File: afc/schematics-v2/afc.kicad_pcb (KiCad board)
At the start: 2 copper layers, 116.8 x 67.3 mm, 16 parts

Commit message: adding v2 schematics
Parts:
- removed ENV2: FAN_H4, Connector:FanPinHeader_1x04_P2.54mm_Vertical
- added Ce: C_Disc_D10.5mm_W5.0mm_P10.00mm, Capacitor_THT:C_Disc_D10.5mm_W5.0mm_P10.00mm, F.Cu at (162.6, 87.5)
- added REF**: R_Axial_DIN0207_L6.3mm_D2.5mm_P10.16mm_Horizontal, Resistor_THT:R_Axial_DIN0207_L6.3mm_D2.5mm_P10.16mm_Horizontal, F.Cu at (135.3, 54.6)
- added REF**: R_Axial_DIN0207_L6.3mm_D2.5mm_P10.16mm_Horizontal, Resistor_THT:R_Axial_DIN0207_L6.3mm_D2.5mm_P10.16mm_Horizontal, F.Cu at (180.3, 77.5)
- added REF**: R_Axial_DIN0207_L6.3mm_D2.5mm_P10.16mm_Horizontal, Resistor_THT:R_Axial_DIN0207_L6.3mm_D2.5mm_P10.16mm_Horizontal, F.Cu at (150.5, 54.6)
- added REF**: R_Axial_DIN0207_L6.3mm_D2.5mm_P10.16mm_Horizontal, Resistor_THT:R_Axial_DIN0207_L6.3mm_D2.5mm_P10.16mm_Horizontal, F.Cu at (120.0, 54.6)
- moved FAN02 27.4 mm to (146.7, 64.8), turned to 180 degrees
- moved FAN03 27.4 mm to (131.4, 64.8), turned to 180 degrees
- moved FAN04 27.4 mm to (116.2, 64.8), turned to 180 degrees
- moved FAN01 27.4 mm to (161.9, 64.8), turned to 180 degrees
- moved ? 20.4 mm to (184.8, 73.7)
- moved ? 20.4 mm to (190.0, 68.6)
- moved ATX2 20.4 mm to (184.8, 83.8)
- moved ATX3 20.4 mm to (184.8, 78.7)
- moved ? 20.4 mm to (184.8, 88.9)
- moved ? 20.4 mm to (190.0, 94.0)
- moved ? 17.0 mm to (108.0, 114.3)
- moved PCIe_MNT_TOP 17.0 mm to (108.0, 76.3)
- moved ESP32_A 14.2 mm to (127.0, 87.6)
- moved ESP32_B 14.0 mm to (127.0, 106.7)
- moved ENV1 8.03 mm to (162.6, 94.0)
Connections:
- ESP32_A pad 1: PWM1 -> TACHO1
- ESP32_A pad 2: TACHO1 -> PWM1
- ESP32_A pad 3: PWM2 -> TACHO2
- ESP32_A pad 4: TACHO2 -> PWM2
- ESP32_A pad 5: PWM3 -> TACHO3
- ESP32_A pad 6: TACHO3 -> PWM3
- ESP32_B pad 10: SDA_1 -> (no net)
- ESP32_B pad 11: SDA_2 -> (no net)
- ESP32_B pad 12: SCL_2 -> SCL_1
- ESP32_B pad 13: (no net) -> SDA_1
- ESP32_B pad 9: SCL_1 -> (no net)
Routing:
- net 12V: track 226.4 -> 121.2 mm
- net SDA_2: track 74.7 -> 0.00 mm
- net GND: track 245.7 -> 172.7 mm
- net SCL_2: track 68.5 -> 0.00 mm
- net TACHO2: track 72.4 -> 25.8 mm
- net TACHO1: track 84.4 -> 38.2 mm
- net PWM1: track 81.6 -> 37.4 mm
- net PWM2: track 69.6 -> 25.8 mm
- net TACHO3: track 60.0 -> 24.2 mm
- net 3V3: track 60.2 -> 25.2 mm
- net PWM3: track 57.9 -> 24.2 mm
- net SDA_1: track 53.0 -> 24.7 mm
- net TACHO4: track 82.8 -> 54.7 mm
- net SCL_1: track 57.7 -> 29.7 mm
- net PWM4: track 68.0 -> 54.7 mm
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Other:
- board size 116.8 x 67.3 mm -> 90.2 x 67.3 mm
- board text removed: "ESP32-S3-ZERO"

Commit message: improvements on PCB design
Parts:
- moved REF** 22.7 mm to (140.3, 64.8), turned to 180 degrees
- moved REF** 22.7 mm to (155.6, 64.8), turned to 180 degrees
- moved REF** 22.7 mm to (170.8, 64.8), turned to 180 degrees
- moved FAN03 13.2 mm to (142.2, 57.1)
- moved FAN04 13.2 mm to (127.0, 57.1)
- moved FAN01 13.2 mm to (172.7, 57.1)
- moved FAN02 13.2 mm to (157.5, 57.1)
- moved ENV1 13.0 mm to (175.3, 91.4)
- moved PCIe_MNT_TOP 9.24 mm to (113.0, 68.6)
- moved ? 9.16 mm to (113.0, 106.7)
- moved ? 6.38 mm to (190.6, 87.6)
- moved ? 6.38 mm to (185.4, 82.5)
- moved ESP32_B 6.38 mm to (127.6, 100.3)
- moved ? 6.38 mm to (190.6, 62.2)
- moved ESP32_A 6.38 mm to (127.7, 81.3)
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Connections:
- REF** pad 1: GND -> 12V (x3)
- REF** pad 2: GND -> 12V (x3)
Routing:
- net 12V: track 121.2 -> 73.6 mm
- net 3V3: track 25.2 -> 39.9 mm
- net SDA_1: track 24.7 -> 36.9 mm
- net SCL_1: track 29.7 -> 41.2 mm
- net TACHO2: track 25.8 -> 37.2 mm
- net PWM2: track 25.8 -> 37.2 mm
- net TACHO1: track 38.2 -> 48.1 mm
- net PWM1: track 37.4 -> 47.3 mm
- net TACHO4: track 54.7 -> 46.6 mm
- net PWM4: track 54.7 -> 46.6 mm
- net PWM3: track 24.2 -> 27.0 mm
- net TACHO3: track 24.2 -> 27.0 mm
- net 5V: track 65.4 -> 66.9 mm
- net GND: track 172.7 -> 173.6 mm
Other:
- board size 90.2 x 67.3 mm -> 85.1 x 59.7 mm

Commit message: more cleanup
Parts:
- moved ENV1 3.59 mm to (172.7, 88.9)
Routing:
- net 5V: track 66.9 -> 76.9 mm
- net 12V: track 73.6 -> 82.8 mm
- net GND: track 173.6 -> 182.7 mm
- net 3V3: track 39.9 -> 48.9 mm
- net SDA_1: track 36.9 -> 33.3 mm
- net SCL_1: track 41.2 -> 37.6 mm
- net TACHO1: track 48.1 -> 47.3 mm
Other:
- outline, holes or cut-outs redrawn

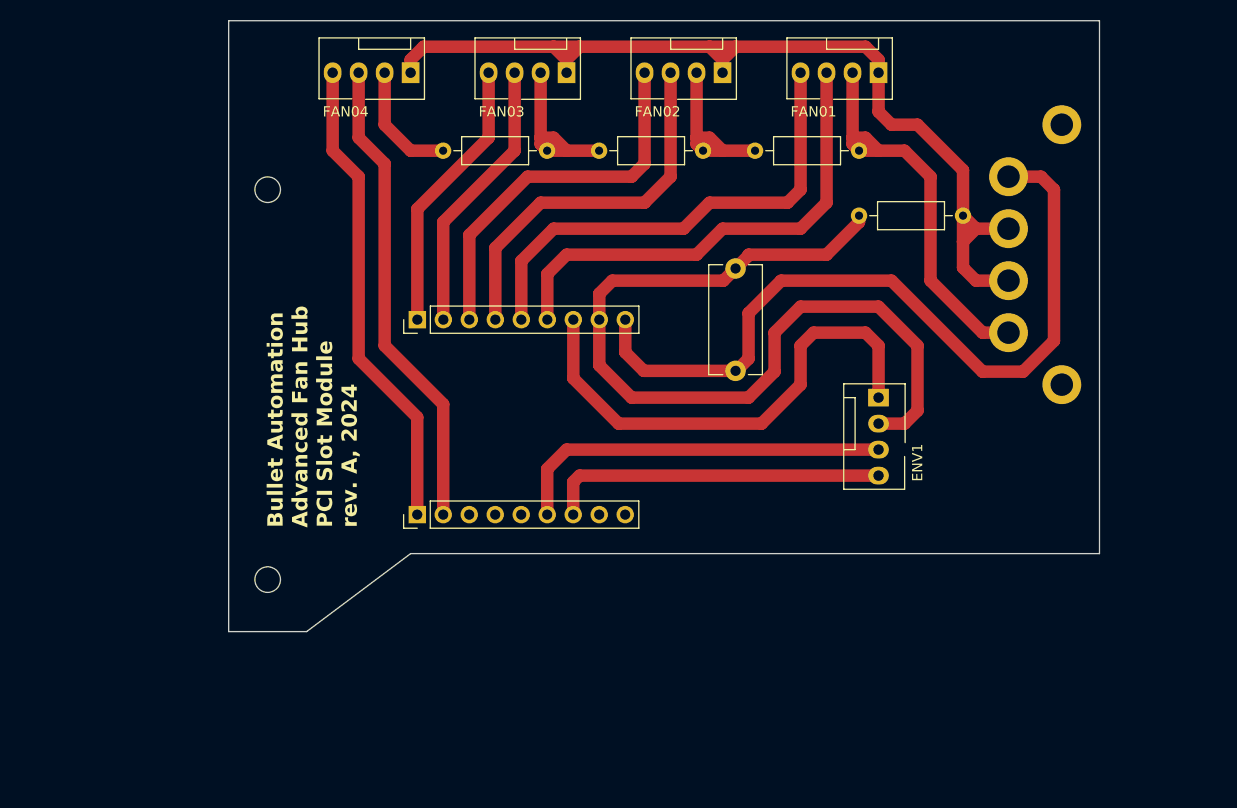
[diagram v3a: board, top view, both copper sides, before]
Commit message: ground plane for schematic
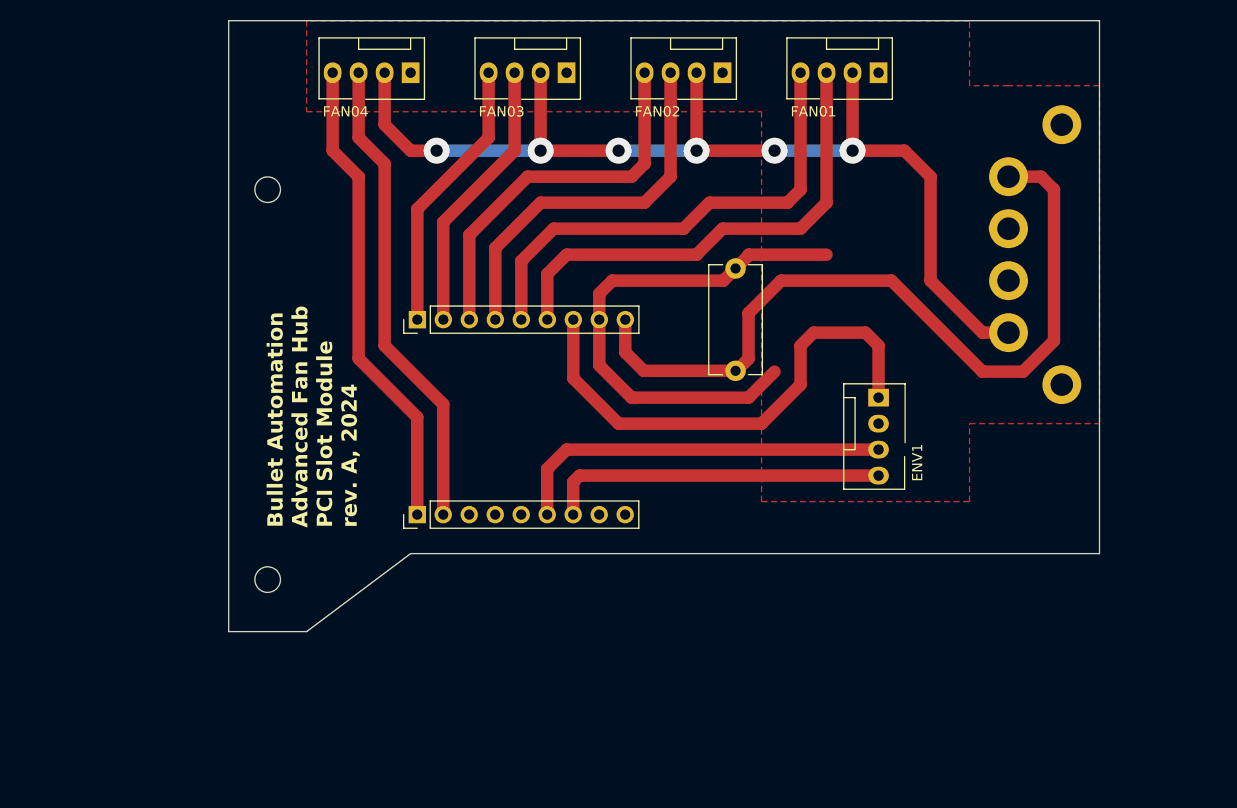
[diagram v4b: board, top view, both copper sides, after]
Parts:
- removed REF** (x4): R_Axial_DIN0207_L6.3mm_D2.5mm_P10.16mm_Horizontal, Resistor_THT:R_Axial_DIN0207_L6.3mm_D2.5mm_P10.16mm_Horizontal
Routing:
- net GND: track 182.7 -> 51.7 mm
- net 12V: track 82.8 -> 103.3 mm, vias 0 -> 6
- added copper zone on F.Cu, net GND

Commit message: updating schematic
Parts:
- moved ESP32_B 3.81 mm to (127.6, 96.5)
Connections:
- ESP32_B pad 12: SCL_1 -> SDA_1
- ESP32_B pad 13: SDA_1 -> SCL_1
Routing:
- net SCL_1: track 37.6 -> 32.0 mm
- net TACHO4: track 46.6 -> 42.8 mm
- net PWM4: track 46.6 -> 42.8 mm
- net SDA_1: track 33.3 -> 37.0 mm
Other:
- board text added: "AFC R2 - Bullet Automation"
- board text removed: "Bullet Automation Advanced Fan Hub PCI Slot Module rev. A, 2024"
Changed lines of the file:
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@@
 	(footprint "Connector_PinHeader_2.54mm:PinHeader_1x09_P2.54mm_Vertical"
 		(layer "F.Cu")
-		(at 127.645 100.33 90)
+		(at 127.645 96.52 90)
 		(descr "Through hole straight pin header, 1x09, 2.54mm pitch, single row")
 		(tags "Through hole pin header THT 1x09 2.54mm single row")
@@
 			(layers "*.Cu" "*.Mask")
 			(remove_unused_layers no)
-			(net 13 "SCL_1")
+			(net 14 "SDA_1")
 		)
 		(pad "13" thru_hole oval
@@
 			(layers "*.Cu" "*.Mask")
 			(remove_unused_layers no)
-			(net 14 "SDA_1")
+			(net 13 "SCL_1")
 		)
 		(pad "RX" thru_hole oval
@@
 		)
 	)
-	(gr_text "Bullet Automation\nAdvanced Fan Hub\nPCI Slot Module\nrev. A, 2024"
-		(at 121.92 101.6 90)
+	(gr_text "AFC R2 - Bullet Automation"
+		(at 116.84 102.87 90)
 		(layer "F.SilkS")
 		(effects
@@
 	)
 	(segment
-		(start 127.645 90.815)
-		(end 127.645 100.33)
+		(start 119.38 64.77)
+		(end 121.92 67.31)
 		(width 1.22)
 		(layer "F.Cu")
@@
 	)
 	(segment
-		(start 121.92 67.31)
-		(end 121.92 85.09)
+		(start 127.645 90.815)
+		(end 127.645 96.52)
 		(width 1.22)
 		(layer "F.Cu")
@@
 	)
 	(segment
-		(start 119.38 57.15)
-		(end 119.38 64.77)
+		(start 121.92 67.31)
+		(end 121.92 85.09)
 		(width 1.22)
 		(layer "F.Cu")
@@
 	)
 	(segment
-		(start 119.38 64.77)
-		(end 121.92 67.31)
+		(start 121.92 85.09)
+		(end 127.645 90.815)
 		(width 1.22)
 		(layer "F.Cu")
@@
 	)
 	(segment
-		(start 121.92 85.09)
-		(end 127.645 90.815)
+		(start 119.38 57.15)
+		(end 119.38 64.77)
 		(width 1.22)
 		(layer "F.Cu")
@@
 	)
 	(segment
-		(start 130.185 100.33)
-		(end 130.185 89.545)
+		(start 121.92 63.5)
+		(end 121.92 57.15)
 		(width 1.22)
 		(layer "F.Cu")
@@
 	)
 	(segment
-		(start 130.185 89.545)
-		(end 124.46 83.82)
+		(start 124.46 83.82)
+		(end 124.46 66.04)
 		(width 1.22)
 		(layer "F.Cu")
@@
 	)
 	(segment
-		(start 124.46 66.04)
-		(end 121.92 63.5)
+		(start 130.185 96.52)
+		(end 130.185 89.545)
 		(width 1.22)
 		(layer "F.Cu")
@@
 	)
 	(segment
-		(start 121.92 63.5)
-		(end 121.92 57.15)
+		(start 130.185 89.545)
+		(end 124.46 83.82)
 		(width 1.22)
 		(layer "F.Cu")
@@
 	)
 	(segment
-		(start 124.46 83.82)
-		(end 124.46 66.04)
+		(start 124.46 66.04)
+		(end 121.92 63.5)
 		(width 1.22)
 		(layer "F.Cu")
@@
 	)
 	(segment
-		(start 140.345 100.33)
-		(end 140.345 95.875)
+		(start 143.51 93.98)
+		(end 172.72 93.98)
 		(width 1.22)
 		(layer "F.Cu")
@@
 	)
 	(segment
-		(start 142.24 93.98)
-		(end 172.72 93.98)
+		(start 142.885 96.52)
+		(end 142.885 94.605)
 		(width 1.22)
 		(layer "F.Cu")
@@
 	)
 	(segment
-		(start 140.345 95.875)
-		(end 142.24 93.98)
+		(start 142.885 94.605)
+		(end 143.51 93.98)
 		(width 1.22)
 		(layer "F.Cu")
@@
 	)
 	(segment
-		(start 143.51 96.52)
-		(end 172.72 96.52)
+		(start 154.94 96.52)
+		(end 151.13 100.33)
+		(width 1.22)
+		(layer "F.Cu")
+		(net 14)
+	)
+	(segment
+		(start 172.72 96.52)
+		(end 154.94 96.52)
 		(width 1.22)
 		(layer "F.Cu")
@@
 	)
 	(segment
-		(start 142.885 97.145)
-		(end 143.51 96.52)
+		(start 140.345 99.08)
+		(end 141.595 100.33)
 		(width 1.22)
 		(layer "F.Cu")
@@
 	)
 	(segment
-		(start 142.885 100.33)
-		(end 142.885 97.145)
+		(start 151.13 100.33)
+		(end 141.595 100.33)
+		(width 1.22)
+		(layer "F.Cu")
+		(net 14)
+	)
+	(segment
+		(start 140.345 96.52)
+		(end 140.345 99.08)
 		(width 1.22)
 		(layer "F.Cu")
@@
 		(name "$teardrop_padvia$")
 		(hatch full 0.1)
-		(priority 30005)
+		(priority 30008)
 		(attr
 			(teardrop
@@
 		(polygon
 			(pts
-				(xy 127.27 64.16) (xy 127.27 65.38) (xy 128.786001 65.77) (xy 129.541 64.77) (xy 128.786001 63.77)
+				(xy 155.55 62.519294) (xy 154.33 62.519294) (xy 153.94 64.000639) (xy 154.94 64.771) (xy 155.94 64.000639)
 			)
 		)
@@
 		(name "$teardrop_padvia$")
 		(hatch full 0.1)
-		(priority 30003)
+		(priority 30005)
 		(attr
 			(teardrop
@@
 		(polygon
 			(pts
-				(xy 157.21 65.38) (xy 157.21 64.16) (xy 155.693999 63.77) (xy 154.939 64.77) (xy 155.693999 65.77)
+				(xy 160.29 64.16) (xy 160.29 65.38) (xy 161.806001 65.77) (xy 162.561 64.77) (xy 161.806001 63.77)
 			)
 		)
@@
 		(name "$teardrop_padvia$")
 		(hatch full 0.1)
-		(priority 30004)
+		(priority 30001)
 		(attr
 			(teardrop
@@
 		(polygon
 			(pts
-				(xy 172.45 65.38) (xy 172.45 64.16) (xy 170.933999 63.77) (xy 170.179 64.77) (xy 170.933999 65.77)
+				(xy 145.05 64.16) (xy 145.05 65.38) (xy 146.566001 65.77) (xy 147.321 64.77) (xy 146.566001 63.77)
 			)
 		)
@@
 		(name "$teardrop_padvia$")
 		(hatch full 0.1)
-		(priority 30007)
+		(priority 30002)
 		(attr
 			(teardrop
@@
 		(polygon
 			(pts
-				(xy 155.55 62.519294) (xy 154.33 62.519294) (xy 153.94 64.000639) (xy 154.94 64.771) (xy 155.94 64.000639)
+				(xy 141.97 65.38) (xy 141.97 64.16) (xy 140.453999 63.77) (xy 139.699 64.77) (xy 140.453999 65.77)
 			)
 		)
@@
 		(name "$teardrop_padvia$")
 		(hatch full 0.1)
-		(priority 30002)
+		(priority 30007)
 		(attr
 			(teardrop
@@
 		(polygon
 			(pts
-				(xy 160.29 64.16) (xy 160.29 65.38) (xy 161.806001 65.77) (xy 162.561 64.77) (xy 161.806001 63.77)
+				(xy 170.79 62.519294) (xy 169.57 62.519294) (xy 169.18 64.000639) (xy 170.18 64.771) (xy 171.18 64.000639)
 			)
 		)
@@
 		(name "$teardrop_padvia$")
 		(hatch full 0.1)
-		(priority 30000)
+		(priority 30003)
 		(attr
 			(teardrop
@@
 		(polygon
 			(pts
-				(xy 145.05 64.16) (xy 145.05 65.38) (xy 146.566001 65.77) (xy 147.321 64.77) (xy 146.566001 63.77)
-			)
-		)
-	)
-	(zone
-		(net 1)
-		(net_name "GND")
-		(layer "F.Cu")
-		(hatch edge 0.5)
-		(connect_pads
-			(clearance 0.75)
-		)
-		(min_thickness 0.25)
-		(filled_areas_thickness no)
-		(fill yes
-			(thermal_gap 0.5)
-			(thermal_bridge_width 0.5)
-		)
-		(polygon
-			(pts
-				(xy 161.29 99.06) (xy 181.61 99.06) (xy 181.61 91.44) (xy 194.31 91.44) (xy 194.31 58.42) (xy 185.42 58.42)
-				(xy 181.61 58.42) (xy 181.61 52.07) (xy 116.84 52.07) (xy 116.84 60.96) (xy 161.29 60.96)
+				(xy 172.45 65.38) (xy 172.45 64.16) (xy 170.933999 63.77) (xy 170.179 64.77) (xy 170.933999 65.77)
 			)
 		)
@@
 		(name "$teardrop_padvia$")
 		(hatch full 0.1)
-		(priority 30006)
+		(priority 30004)
 		(attr
 			(teardrop
@@
 		(polygon
 			(pts
-				(xy 140.31 62.519294) (xy 139.09 62.519294) (xy 138.7 64.000639) (xy 139.7 64.771) (xy 140.7 64.000639)
+				(xy 157.21 65.38) (xy 157.21 64.16) (xy 155.693999 63.77) (xy 154.939 64.77) (xy 155.693999 65.77)
+			)
+		)
+	)
+	(zone
+		(net 1)
+		(net_name "GND")
+		(layer "F.Cu")
+		(hatch edge 0.5)
+		(connect_pads
+			(clearance 0.75)
+		)
+		(min_thickness 0.25)
+		(filled_areas_thickness no)
+		(fill yes
+			(thermal_gap 0.5)
+			(thermal_bridge_width 0.5)
+		)
+		(polygon
+			(pts
+				(xy 161.29 102.87) (xy 181.61 102.87) (xy 181.61 96.52) (xy 194.31 96.52) (xy 194.31 58.42) (xy 185.42 58.42)
+				(xy 181.61 58.42) (xy 181.61 52.07) (xy 118.11 52.07) (xy 118.11 76.2) (xy 118.11 102.87)
 			)
 		)
@@
 		(name "$teardrop_padvia$")
 		(hatch full 0.1)
-		(priority 30001)
+		(priority 30000)
 		(attr
 			(teardrop
@@
 		(polygon
 			(pts
-				(xy 141.97 65.38) (xy 141.97 64.16) (xy 140.453999 63.77) (xy 139.699 64.77) (xy 140.453999 65.77)
+				(xy 127.27 64.16) (xy 127.27 65.38) (xy 128.786001 65.77) (xy 129.541 64.77) (xy 128.786001 63.77)
 			)
 		)
@@
 		(name "$teardrop_padvia$")
 		(hatch full 0.1)
-		(priority 30008)
+		(priority 30006)
 		(attr
 			(teardrop
@@
 		(polygon
 			(pts
-				(xy 170.79 62.519294) (xy 169.57 62.519294) (xy 169.18 64.000639) (xy 170.18 64.771) (xy 171.18 64.000639)
+				(xy 140.31 62.519294) (xy 139.09 62.519294) (xy 138.7 64.000639) (xy 139.7 64.771) (xy 140.7 64.000639)
 			)
 		)
@@
 		(name "$teardrop_padvia$")
 		(hatch full 0.1)
-		(priority 30002)
+		(priority 30001)
 		(attr
 			(teardrop
@@
 		(polygon
 			(pts
-				(xy 149.59 65.38) (xy 149.59 64.16) (xy 148.073999 63.77) (xy 147.319 64.77) (xy 148.073999 65.77)
+				(xy 152.67 64.16) (xy 152.67 65.38) (xy 154.186001 65.77) (xy 154.941 64.77) (xy 154.186001 63.77)
 			)
 		)
@@
 		(polygon
 			(pts
-				(xy 137.43 64.16) (xy 137.43 65.38) (xy 138.946001 65.77) (xy 139.701 64.77) (xy 138.946001 63.77)
+				(xy 164.83 65.38) (xy 164.83 64.16) (xy 163.313999 63.77) (xy 162.559 64.77) (xy 163.313999 65.77)
 			)
 		)
@@
 		(name "$teardrop_padvia$")
 		(hatch full 0.1)
-		(priority 30000)
+		(priority 30004)
 		(attr
 			(teardrop
@@
 		(polygon
 			(pts
-				(xy 164.83 65.38) (xy 164.83 64.16) (xy 163.313999 63.77) (xy 162.559 64.77) (xy 163.313999 65.77)
+				(xy 167.91 64.16) (xy 167.91 65.38) (xy 169.426001 65.77) (xy 170.181 64.77) (xy 169.426001 63.77)
 			)
 		)
@@
 		(name "$teardrop_padvia$")
 		(hatch full 0.1)
-		(priority 30001)
+		(priority 30003)
 		(attr
 			(teardrop
@@
 		(polygon
 			(pts
-				(xy 167.91 64.16) (xy 167.91 65.38) (xy 169.426001 65.77) (xy 170.181 64.77) (xy 169.426001 63.77)
+				(xy 137.43 64.16) (xy 137.43 65.38) (xy 138.946001 65.77) (xy 139.701 64.77) (xy 138.946001 63.77)
 			)
 		)
@@
 		(name "$teardrop_padvia$")
 		(hatch full 0.1)
-		(priority 30004)
+		(priority 30002)
 		(attr
 			(teardrop
@@
 		(name "$teardrop_padvia$")
 		(hatch full 0.1)
-		(priority 30003)
+		(priority 30000)
 		(attr
 			(teardrop
@@
 		(polygon
 			(pts
-				(xy 152.67 64.16) (xy 152.67 65.38) (xy 154.186001 65.77) (xy 154.941 64.77) (xy 154.186001 63.77)
+				(xy 149.59 65.38) (xy 149.59 64.16) (xy 148.073999 63.77) (xy 147.319 64.77) (xy 148.073999 65.77)
 			)
 		)
